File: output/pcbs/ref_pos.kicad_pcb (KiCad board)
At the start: 2 copper layers, 125.8 x 86.6 mm, 0 parts

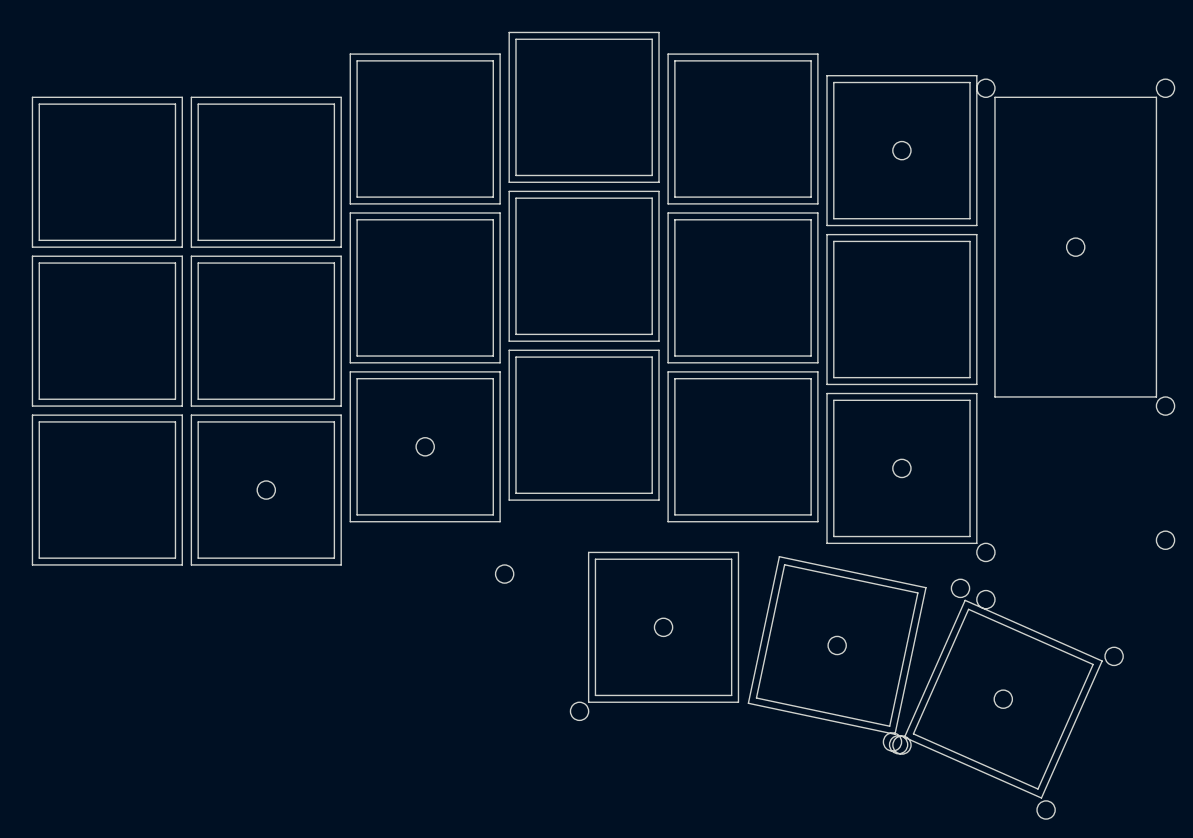
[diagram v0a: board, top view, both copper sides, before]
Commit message: feat: add more ref pos (9-14) and ref corners
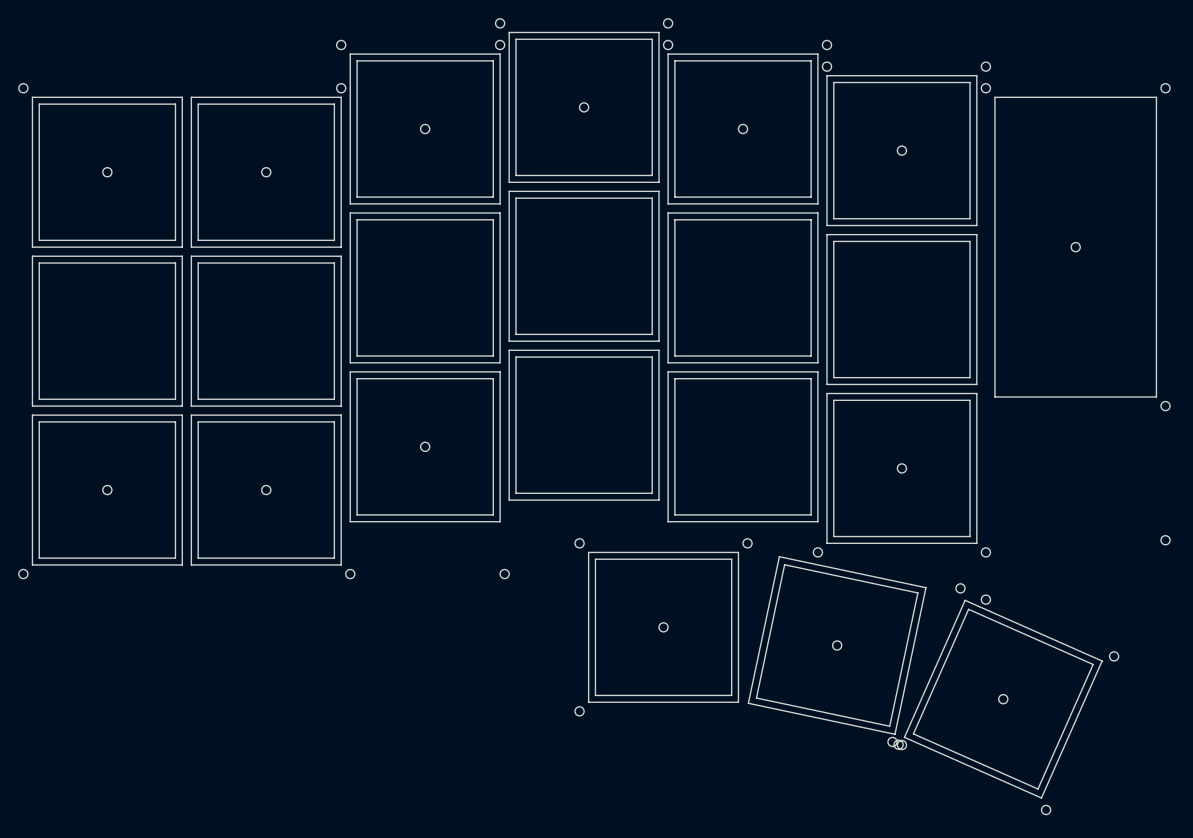
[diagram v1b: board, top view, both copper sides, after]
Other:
- board size 125.8 x 86.6 mm -> 126.8 x 87.6 mm
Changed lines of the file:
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@@
   (title_block
     (title "ref_pos")
-    (date "2025-01-07")
+    (date "2025-01-11")
     (rev "v1.0.0")
     (company "Unknown")
@@
 (gr_line (start 115.53 -43.25) (end 97.75 -43.25) (layer Edge.Cuts) (stroke (width 0.15) (type default)))
 (gr_line (start 97.75 -43.25) (end 97.75 -10.25) (layer Edge.Cuts) (stroke (width 0.15) (type default)))
-(gr_circle (center 17.5 0) (end 18.5 0) (layer Edge.Cuts) (stroke (width 0.15) (type default)) (fill none))
-(gr_circle (center 87.5 -2.381) (end 88.5 -2.381) (layer Edge.Cuts) (stroke (width 0.15) (type default)) (fill none))
-(gr_circle (center 61.25 15.119) (end 62.25 15.119) (layer Edge.Cuts) (stroke (width 0.15) (type default)) (fill none))
-(gr_circle (center 80.37095550000001 17.1185716) (end 81.37095550000001 17.1185716) (layer Edge.Cuts) (stroke (width 0.15) (type default)) (fill none))
-(gr_circle (center 98.6645391 23.0307643) (end 99.6645391 23.0307643) (layer Edge.Cuts) (stroke (width 0.15) (type default)) (fill none))
-(gr_circle (center 87.5 -37.381) (end 88.5 -37.381) (layer Edge.Cuts) (stroke (width 0.15) (type default)) (fill none))
-(gr_circle (center 106.64 -26.75) (end 107.64 -26.75) (layer Edge.Cuts) (stroke (width 0.15) (type default)) (fill none))
-(gr_circle (center 35 -4.762) (end 36 -4.762) (layer Edge.Cuts) (stroke (width 0.15) (type default)) (fill none))
-(gr_circle (center 96.75 6.869) (end 97.75 6.869) (layer Edge.Cuts) (stroke (width 0.15) (type default)) (fill none))
-(gr_circle (center 52 24.369) (end 53 24.369) (layer Edge.Cuts) (stroke (width 0.15) (type default)) (fill none))
-(gr_circle (center 87.5071226 28.0821531) (end 88.5071226 28.0821531) (layer Edge.Cuts) (stroke (width 0.15) (type default)) (fill none))
-(gr_circle (center 103.3780884 35.2335285) (end 104.3780884 35.2335285) (layer Edge.Cuts) (stroke (width 0.15) (type default)) (fill none))
-(gr_circle (center 86.4617749 27.7443136) (end 87.4617749 27.7443136) (layer Edge.Cuts) (stroke (width 0.15) (type default)) (fill none))
-(gr_circle (center 110.8673033 18.317215) (end 111.8673033 18.317215) (layer Edge.Cuts) (stroke (width 0.15) (type default)) (fill none))
-(gr_circle (center 93.9509898 10.8280001) (end 94.9509898 10.8280001) (layer Edge.Cuts) (stroke (width 0.15) (type default)) (fill none))
-(gr_circle (center 116.53 -9.25) (end 117.53 -9.25) (layer Edge.Cuts) (stroke (width 0.15) (type default)) (fill none))
-(gr_circle (center 116.53 -44.25) (end 117.53 -44.25) (layer Edge.Cuts) (stroke (width 0.15) (type default)) (fill none))
-(gr_circle (center 96.75 -44.25) (end 97.75 -44.25) (layer Edge.Cuts) (stroke (width 0.15) (type default)) (fill none))
-(gr_circle (center 43.75 9.25) (end 44.75 9.25) (layer Edge.Cuts) (stroke (width 0.15) (type default)) (fill none))
-(gr_circle (center 96.75 12.067182) (end 97.75 12.067182) (layer Edge.Cuts) (stroke (width 0.15) (type default)) (fill none))
-(gr_circle (center 87.1375839 28.0435087) (end 88.1375839 28.0435087) (layer Edge.Cuts) (stroke (width 0.15) (type default)) (fill none))
-(gr_circle (center 116.53 5.5265615) (end 117.53 5.5265615) (layer Edge.Cuts) (stroke (width 0.15) (type default)) (fill none))
+(gr_circle (center 17.5 0) (end 18 0) (layer Edge.Cuts) (stroke (width 0.15) (type default)) (fill none))
+(gr_circle (center 87.5 -2.381) (end 88 -2.381) (layer Edge.Cuts) (stroke (width 0.15) (type default)) (fill none))
+(gr_circle (center 61.25 15.119) (end 61.75 15.119) (layer Edge.Cuts) (stroke (width 0.15) (type default)) (fill none))
+(gr_circle (center 80.37095550000001 17.1185716) (end 80.87095550000001 17.1185716) (layer Edge.Cuts) (stroke (width 0.15) (type default)) (fill none))
+(gr_circle (center 98.6645391 23.0307643) (end 99.1645391 23.0307643) (layer Edge.Cuts) (stroke (width 0.15) (type default)) (fill none))
+(gr_circle (center 87.5 -37.381) (end 88 -37.381) (layer Edge.Cuts) (stroke (width 0.15) (type default)) (fill none))
+(gr_circle (center 106.64 -26.75) (end 107.14 -26.75) (layer Edge.Cuts) (stroke (width 0.15) (type default)) (fill none))
+(gr_circle (center 35 -4.762) (end 35.5 -4.762) (layer Edge.Cuts) (stroke (width 0.15) (type default)) (fill none))
+(gr_circle (center 0 0) (end 0.5 0) (layer Edge.Cuts) (stroke (width 0.15) (type default)) (fill none))
+(gr_circle (center 0 -35) (end 0.5 -35) (layer Edge.Cuts) (stroke (width 0.15) (type default)) (fill none))
+(gr_circle (center 17.5 -35) (end 18 -35) (layer Edge.Cuts) (stroke (width 0.15) (type default)) (fill none))
+(gr_circle (center 35 -39.762) (end 35.5 -39.762) (layer Edge.Cuts) (stroke (width 0.15) (type default)) (fill none))
+(gr_circle (center 52.5 -42.143) (end 53 -42.143) (layer Edge.Cuts) (stroke (width 0.15) (type default)) (fill none))
+(gr_circle (center 70 -39.762) (end 70.5 -39.762) (layer Edge.Cuts) (stroke (width 0.15) (type default)) (fill none))
+(gr_circle (center 26.75 9.25) (end 27.25 9.25) (layer Edge.Cuts) (stroke (width 0.15) (type default)) (fill none))
+(gr_circle (center 96.75 6.869) (end 97.25 6.869) (layer Edge.Cuts) (stroke (width 0.15) (type default)) (fill none))
+(gr_circle (center 78.25 6.869) (end 78.75 6.869) (layer Edge.Cuts) (stroke (width 0.15) (type default)) (fill none))
+(gr_circle (center 52 24.369) (end 52.5 24.369) (layer Edge.Cuts) (stroke (width 0.15) (type default)) (fill none))
+(gr_circle (center 52 5.869) (end 52.5 5.869) (layer Edge.Cuts) (stroke (width 0.15) (type default)) (fill none))
+(gr_circle (center 70.5 5.869) (end 71 5.869) (layer Edge.Cuts) (stroke (width 0.15) (type default)) (fill none))
+(gr_circle (center 87.5071226 28.0821531) (end 88.0071226 28.0821531) (layer Edge.Cuts) (stroke (width 0.15) (type default)) (fill none))
+(gr_circle (center 103.3780884 35.2335285) (end 103.8780884 35.2335285) (layer Edge.Cuts) (stroke (width 0.15) (type default)) (fill none))
+(gr_circle (center 86.4617749 27.7443136) (end 86.9617749 27.7443136) (layer Edge.Cuts) (stroke (width 0.15) (type default)) (fill none))
+(gr_circle (center 110.8673033 18.317215) (end 111.3673033 18.317215) (layer Edge.Cuts) (stroke (width 0.15) (type default)) (fill none))
+(gr_circle (center 93.9509898 10.8280001) (end 94.4509898 10.8280001) (layer Edge.Cuts) (stroke (width 0.15) (type default)) (fill none))
+(gr_circle (center 79.25 -46.631) (end 79.75 -46.631) (layer Edge.Cuts) (stroke (width 0.15) (type default)) (fill none))
+(gr_circle (center 96.75 -46.631) (end 97.25 -46.631) (layer Edge.Cuts) (stroke (width 0.15) (type default)) (fill none))
+(gr_circle (center 116.53 -9.25) (end 117.03 -9.25) (layer Edge.Cuts) (stroke (width 0.15) (type default)) (fill none))
+(gr_circle (center 116.53 -44.25) (end 117.03 -44.25) (layer Edge.Cuts) (stroke (width 0.15) (type default)) (fill none))
+(gr_circle (center 96.75 -44.25) (end 97.25 -44.25) (layer Edge.Cuts) (stroke (width 0.15) (type default)) (fill none))
+(gr_circle (center 43.75 9.25) (end 44.25 9.25) (layer Edge.Cuts) (stroke (width 0.15) (type default)) (fill none))
+(gr_circle (center -9.25 9.25) (end -8.75 9.25) (layer Edge.Cuts) (stroke (width 0.15) (type default)) (fill none))
+(gr_circle (center -9.25 -44.25) (end -8.75 -44.25) (layer Edge.Cuts) (stroke (width 0.15) (type default)) (fill none))
+(gr_circle (center 25.75 -44.25) (end 26.25 -44.25) (layer Edge.Cuts) (stroke (width 0.15) (type default)) (fill none))
+(gr_circle (center 25.75 -49.012) (end 26.25 -49.012) (layer Edge.Cuts) (stroke (width 0.15) (type default)) (fill none))
+(gr_circle (center 43.25 -49.012) (end 43.75 -49.012) (layer Edge.Cuts) (stroke (width 0.15) (type default)) (fill none))
+(gr_circle (center 43.25 -51.393) (end 43.75 -51.393) (layer Edge.Cuts) (stroke (width 0.15) (type default)) (fill none))
+(gr_circle (center 61.75 -51.393) (end 62.25 -51.393) (layer Edge.Cuts) (stroke (width 0.15) (type default)) (fill none))
+(gr_circle (center 61.75 -49.012) (end 62.25 -49.012) (layer Edge.Cuts) (stroke (width 0.15) (type default)) (fill none))
+(gr_circle (center 79.25 -49.012) (end 79.75 -49.012) (layer Edge.Cuts) (stroke (width 0.15) (type default)) (fill none))
+(gr_circle (center 96.75 12.067182) (end 97.25 12.067182) (layer Edge.Cuts) (stroke (width 0.15) (type default)) (fill none))
+(gr_circle (center 87.1375839 28.0435087) (end 87.6375839 28.0435087) (layer Edge.Cuts) (stroke (width 0.15) (type default)) (fill none))
+(gr_circle (center 116.53 5.5265615) (end 117.03 5.5265615) (layer Edge.Cuts) (stroke (width 0.15) (type default)) (fill none))
 )

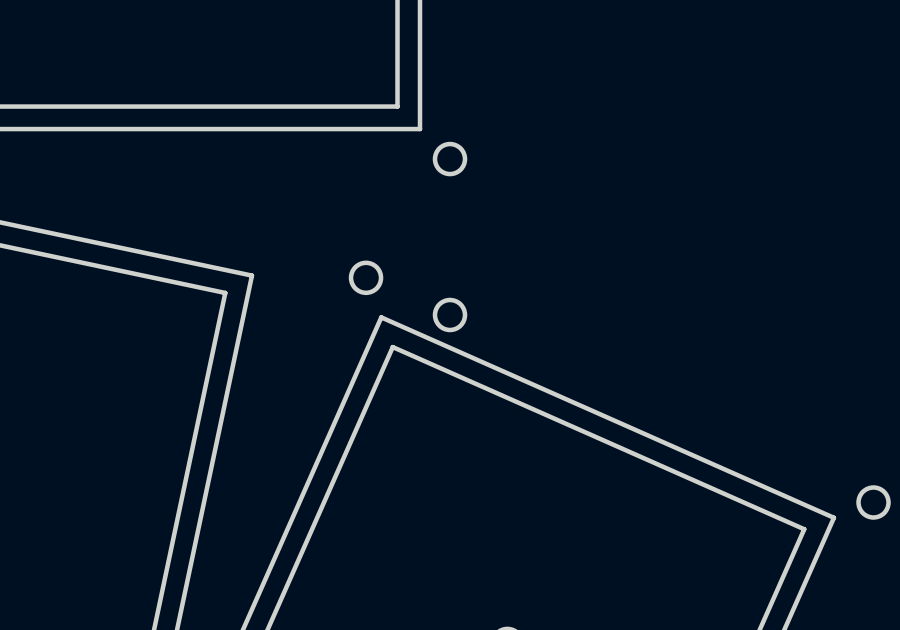
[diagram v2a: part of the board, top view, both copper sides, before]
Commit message: feat: update mcu plate calculations
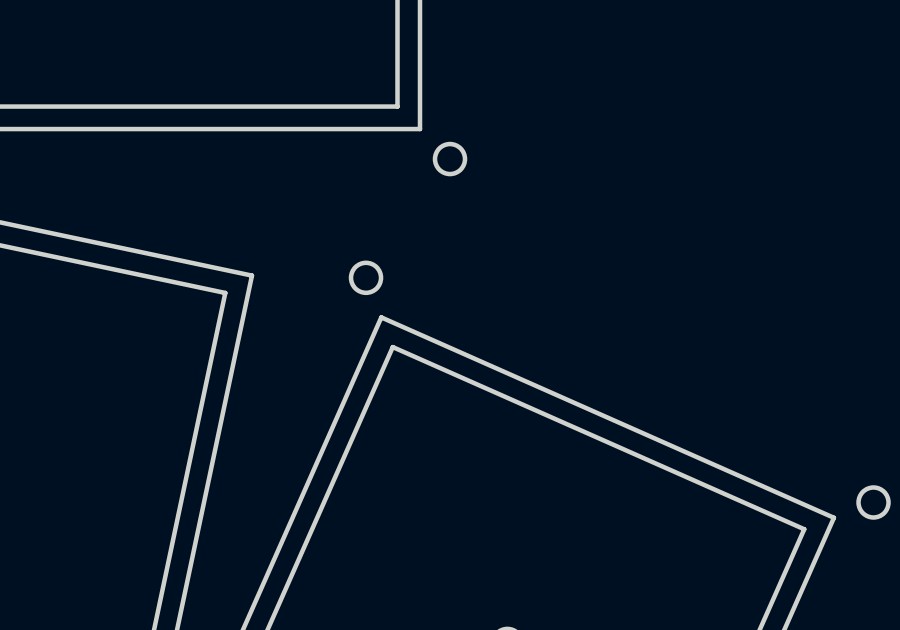
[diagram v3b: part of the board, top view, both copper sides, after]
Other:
- outline, holes or cut-outs redrawn
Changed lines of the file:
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@@
 (gr_circle (center 61.75 -49.012) (end 62.25 -49.012) (layer Edge.Cuts) (stroke (width 0.15) (type default)) (fill none))
 (gr_circle (center 79.25 -49.012) (end 79.75 -49.012) (layer Edge.Cuts) (stroke (width 0.15) (type default)) (fill none))
-(gr_circle (center 96.75 12.067182) (end 97.25 12.067182) (layer Edge.Cuts) (stroke (width 0.15) (type default)) (fill none))
 (gr_circle (center 87.1375839 28.0435087) (end 87.6375839 28.0435087) (layer Edge.Cuts) (stroke (width 0.15) (type default)) (fill none))
 (gr_circle (center 116.53 5.5265615) (end 117.03 5.5265615) (layer Edge.Cuts) (stroke (width 0.15) (type default)) (fill none))
